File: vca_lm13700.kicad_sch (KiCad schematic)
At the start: 24 parts

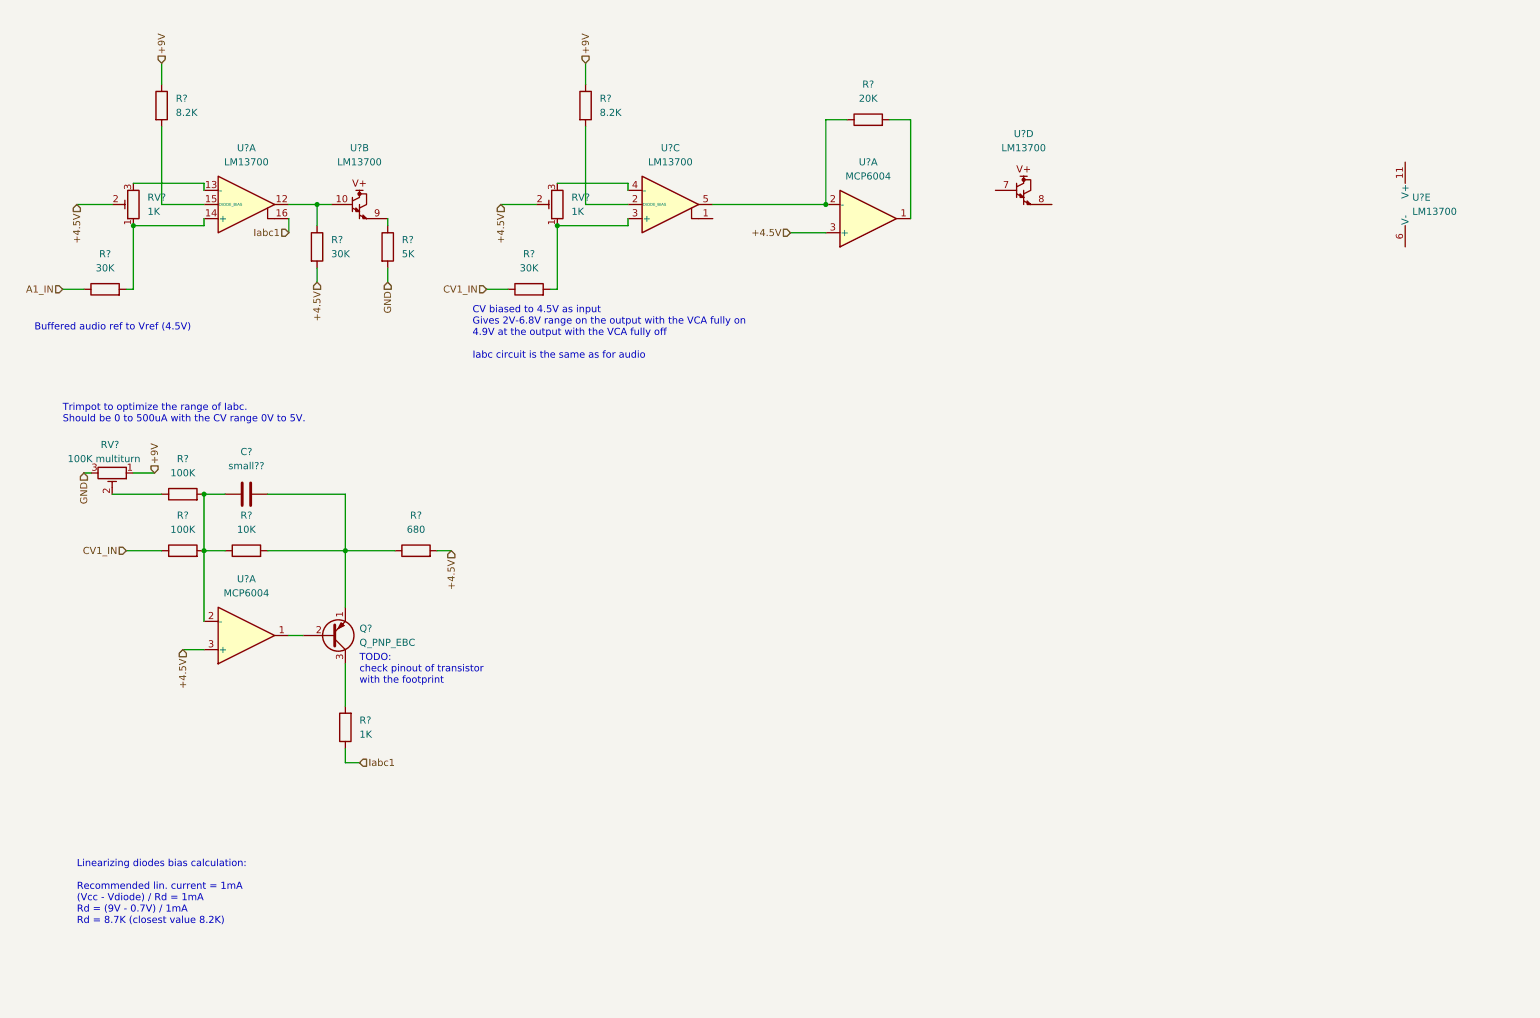
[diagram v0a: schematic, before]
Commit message: Attenuverters laid out
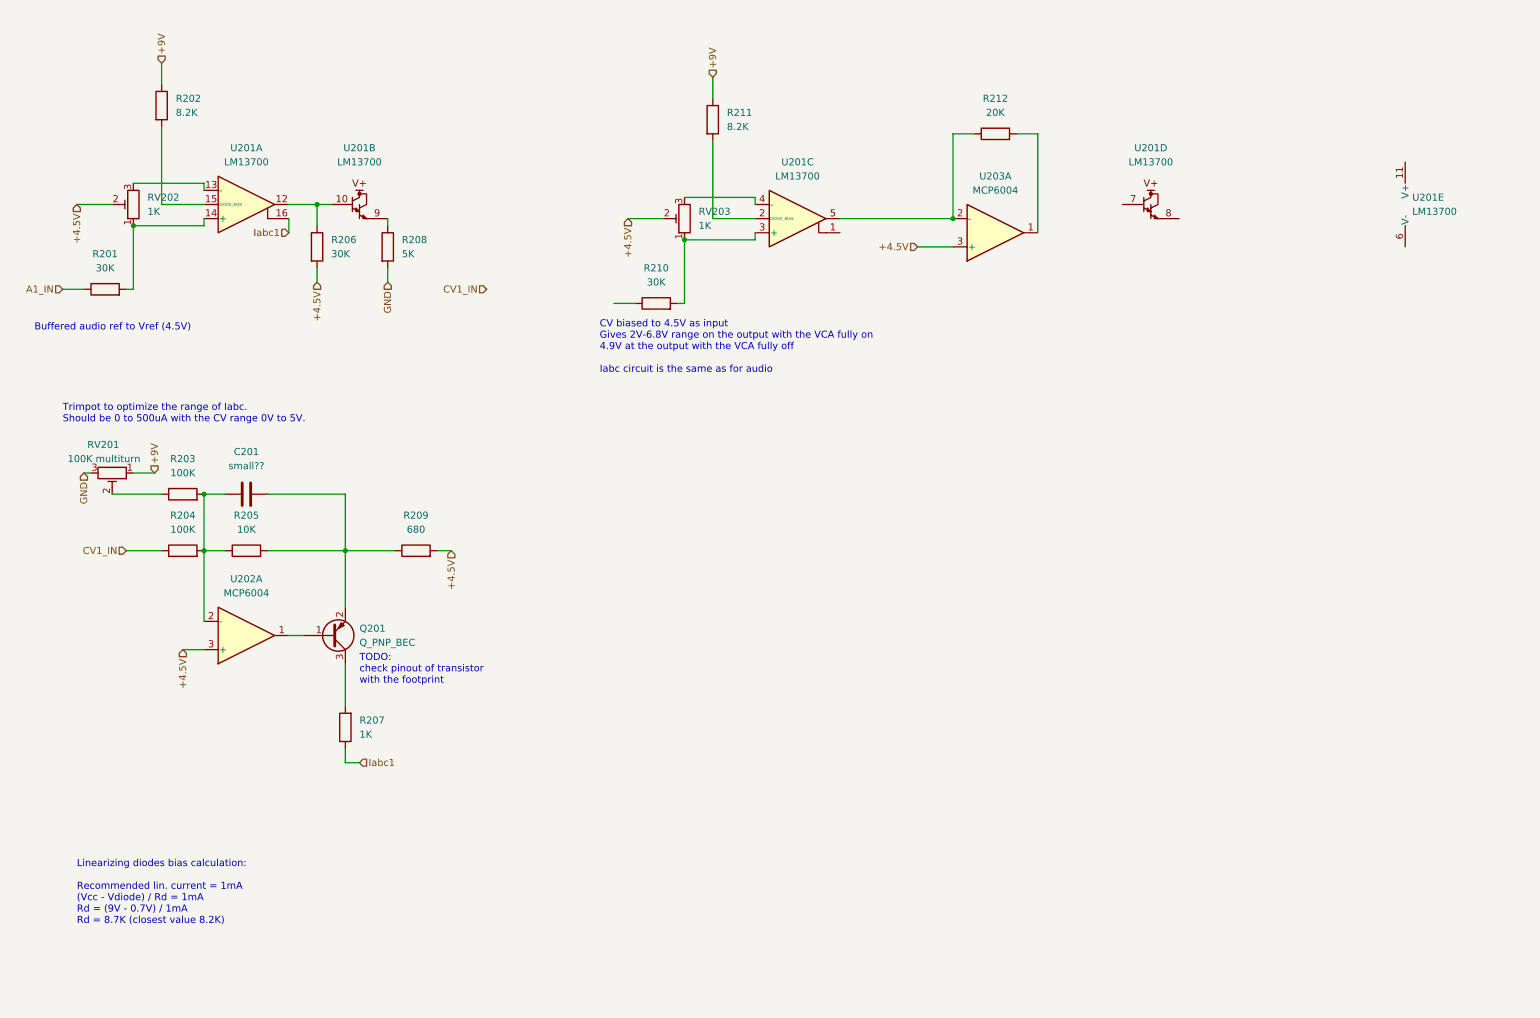
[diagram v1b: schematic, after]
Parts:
- C201: renamed from C?; footprint (none) -> Capacitor_SMD:C_0603_1608Metric_Pad1.08x0.95mm_HandSolder
- Q201: renamed from Q?; value Q_PNP_EBC -> Q_PNP_BEC; footprint (none) -> Package_TO_SOT_SMD:SOT-23_Handsoldering; symbol Device:Q_PNP_EBC -> Device:Q_PNP_BEC
- R201, R202, R203, R204, R205, R206, R207, R208, R209, R210, R211, R212: renamed from R?; footprint (none) -> Resistor_SMD:R_0603_1608Metric_Pad0.98x0.95mm_HandSolder
- RV201, RV202, RV203: renamed from RV?; footprint (none) -> Potentiometer_SMD:Potentiometer_Bourns_3314J_Vertical
- U201: renamed from U?; footprint (none) -> Package_SO:SOIC-16_3.9x9.9mm_P1.27mm
- U202, U203: renamed from U?; footprint (none) -> Package_SO:TSSOP-14_4.4x5mm_P0.65mm
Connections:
- net CV1_IN: no longer R210.1
- net at C201.2, R205.2, R209.1: now also Q201.2 (E); no longer Q201.1 (E)
- net at U202.1: now also Q201.1 (B); no longer Q201.2 (B)
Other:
- moved on the sheet: R210, R211, R212, RV203, U201C, U201D, U203A

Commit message: VCF schem combed
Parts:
- C201: value small?? -> 470p
- U202, U203: footprint Package_SO:TSSOP-14_4.4x5mm_P0.65mm -> Package_SO:SOIC-14_3.9x8.7mm_P1.27mm
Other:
- note added: "Cap sets the LPF cutoff at 34kHz"
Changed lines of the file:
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@@
     (stroke (width 0) (type default) (color 0 0 0 0))
+  )
+  (text "Cap sets the LPF cutoff at 34kHz" (at 59.69 97.79 0)
+    (effects (font (size 1.27 1.27)) (justify left bottom))
   )
   (text "TODO:\ncheck pinout of transistor\nwith the footprint"
@@
     (property "Reference" "U203" (id 0) (at 190.5 43.18 0))
     (property "Value" "MCP6004" (id 1) (at 190.5 45.72 0))
-    (property "Footprint" "Package_SO:TSSOP-14_4.4x5mm_P0.65mm" (id 2) (at 189.23 55.88 0)
+    (property "Footprint" "Package_SO:SOIC-14_3.9x8.7mm_P1.27mm" (id 2) (at 189.23 55.88 0)
       (effects (font (size 1.27 1.27)) hide)
     )
@@
     (in_bom yes) (on_board yes) (fields_autoplaced)
     (property "Reference" "C201" (id 0) (at 55.88 92.71 90))
-    (property "Value" "small??" (id 1) (at 55.88 95.25 90))
+    (property "Value" "470p" (id 1) (at 55.88 95.25 90))
     (property "Footprint" "Capacitor_SMD:C_0603_1608Metric_Pad1.08x0.95mm_HandSolder" (id 2) (at 59.69 99.3648 0)
       (effects (font (size 1.27 1.27)) hide)
@@
     (property "Reference" "U202" (id 0) (at 55.88 115.57 0))
     (property "Value" "MCP6004" (id 1) (at 55.88 118.11 0))
-    (property "Footprint" "Package_SO:TSSOP-14_4.4x5mm_P0.65mm" (id 2) (at 54.61 128.27 0)
-      (effects (font (size 1.27 1.27)) hide)
-    )
+    (property "Footprint" "Package_SO:SOIC-14_3.9x8.7mm_P1.27mm" (id 2) (at 54.61 128.27 0)
+      (effects (font (size 1.27 1.27)) hide)
+    )

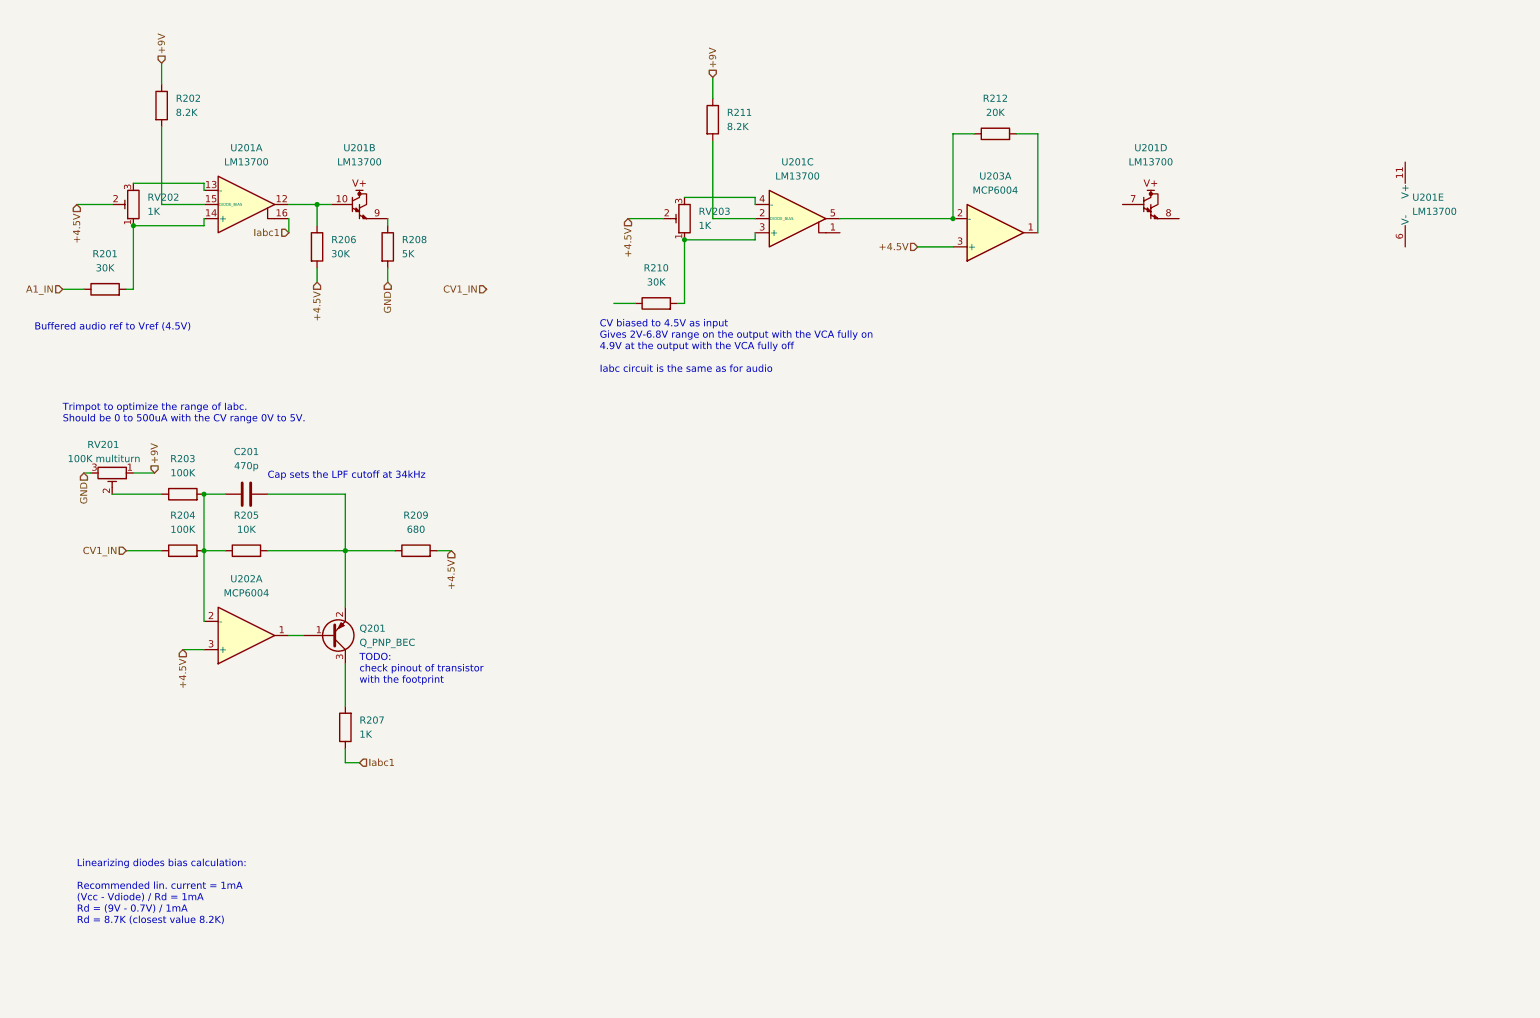
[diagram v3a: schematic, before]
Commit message: VCF layout done, vca capture
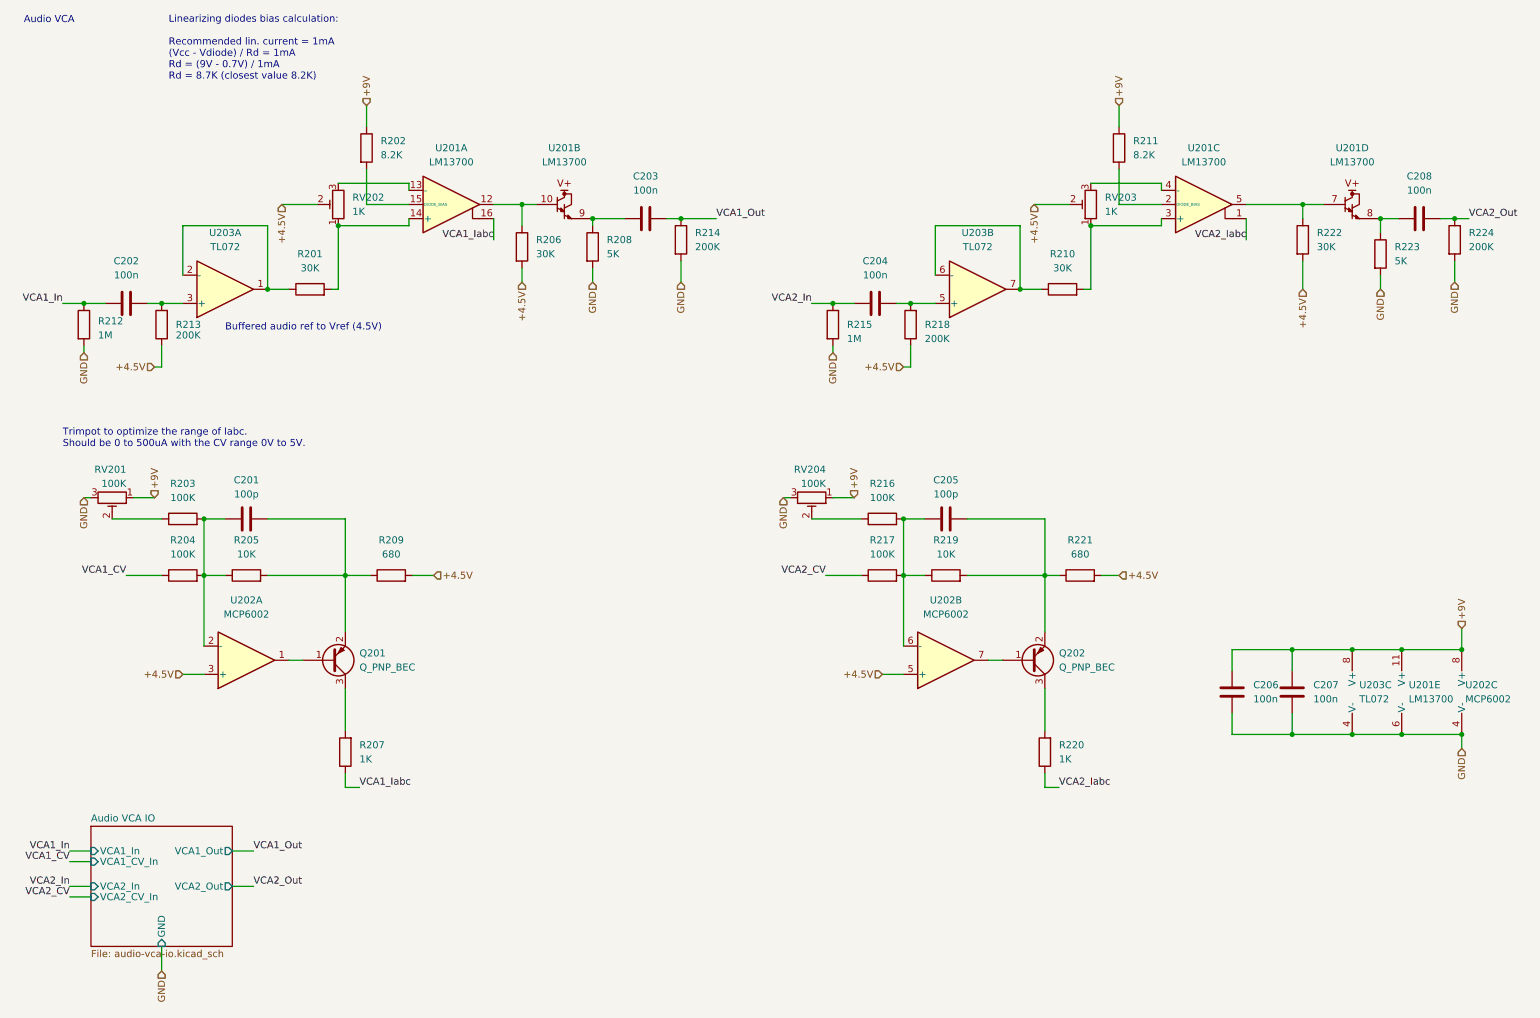
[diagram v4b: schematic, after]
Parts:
- removed U202, U203: MCP6004, Package_SO:SOIC-14_3.9x8.7mm_P1.27mm, symbol Amplifier_Operational:MCP6004
- added C202, C203, C204, C206, C207, C208: 100n, Capacitor_SMD:C_0603_1608Metric_Pad1.08x0.95mm_HandSolder, symbol Device:C
- added C205: 100p, Capacitor_SMD:C_0603_1608Metric_Pad1.08x0.95mm_HandSolder, symbol Device:C
- added Q202: Q_PNP_BEC, Package_TO_SOT_SMD:SOT-23_Handsoldering, symbol Device:Q_PNP_BEC
- added R213, R214, R218, R224: 200K, Resistor_SMD:R_0603_1608Metric_Pad0.98x0.95mm_HandSolder, symbol Device:R
- added R215: 1M, Resistor_SMD:R_0603_1608Metric_Pad0.98x0.95mm_HandSolder, symbol Device:R
- added R216, R217: 100K, Resistor_SMD:R_0603_1608Metric_Pad0.98x0.95mm_HandSolder, symbol Device:R
- added R219: 10K, Resistor_SMD:R_0603_1608Metric_Pad0.98x0.95mm_HandSolder, symbol Device:R
- added R220: 1K, Resistor_SMD:R_0603_1608Metric_Pad0.98x0.95mm_HandSolder, symbol Device:R
- added R221: 680, Resistor_SMD:R_0603_1608Metric_Pad0.98x0.95mm_HandSolder, symbol Device:R
- added R222: 30K, Resistor_SMD:R_0603_1608Metric_Pad0.98x0.95mm_HandSolder, symbol Device:R
- added R223: 5K, Resistor_SMD:R_0603_1608Metric_Pad0.98x0.95mm_HandSolder, symbol Device:R
- added RV204: 100K, Potentiometer_SMD:Potentiometer_Bourns_3314J_Vertical, symbol Device:R_Potentiometer_Trim
- added U202: MCP6002, symbol Amplifier_Operational:MCP6002-xSN
- added U203: TL072, symbol Amplifier_Operational:TL072
- C201: value 470p -> 100p
- R212: value 20K -> 1M
- RV201: value 100K multiturn -> 100K
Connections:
- net +4.5V: now also R213.1, R218.1, R221.2, R222.2, U202.3 (+), U202.5 (+)
- net +9V: now also U201.11 (V+), C206.1, C207.1, RV204.1, U202.8 (V+), U203.8 (V+)
- net GND: now also R212.2, U201.6 (V-), C206.2, C207.2, R214.2, R215.2, R223.2, R224.2, RV204.3, U202.4 (V-), U203.4 (V-)
- net at C201.1, R203.2, R204.2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: now also U202.2 (-)
- net at U201.5: now also U201.7, R222.1; no longer R212.1
- net at R210.1: now also U203.6 (-), U203.7
- net at R208.1, U201.9: now also C203.1
- net at Q201.1 (B): now also U202.1
- net VCA2_Iabc: now reaches U201.1
- net VCA2_Iabc: now also R220.1
- net at U201.8: now also C208.1, R223.1
- net A1_IN: no longer names the net of R201.1
- net A1_IN: now also U203.1, U203.2 (-)
- net CV1_IN renamed VCA1_CV
- net Iabc1 renamed VCA1_Iabc
- new net: R216.1, RV204.2
- new net: C205.1, R216.2, R217.2, R219.1, U202.6 (-)
- new net: Q202.1 (B), U202.7
- new net: C204.2, R218.2, U203.5 (+)
- new net: C205.2, Q202.2 (E), R219.2, R221.1
- new net: Q202.3 (C), R220.2
- new net: C202.2, R213.2, U203.3 (+)
- new net VCA1_In: C202.1, R212.1
- new net VCA1_Out: C203.2, R214.1
- new net VCA2_CV: R217.1
- new net VCA2_In: C204.1, R215.1
- new net VCA2_Out: C208.2, R224.1
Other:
- added sheet Audio VCA IO (audio-vca-io.kicad_sch)
- note added: "Audio VCA"
- note removed: "CV biased to 4.5V as input Gives 2V-6.8V range on the output with the VCA fully on 4.9V at the output with the VCA fully off Iabc circuit is the same as for audio"
- note removed: "Cap sets the LPF cutoff at 34kHz"
- note removed: "TODO: check pinout of transistor with the footprint"
- moved on the sheet: C201, Q201, R201, R202, R203, R204, R205, R206, R207, R208, R209, R210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
